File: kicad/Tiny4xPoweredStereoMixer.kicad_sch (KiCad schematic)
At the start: 15 parts, among them J1 RCJ-2221, J2 RCJ-2221, J3 RCJ-2221, J4 RCJ-2221, J5 RCJ-2221, U3 LM2611AMF/NOPB

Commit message: updates
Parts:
- added C7: 100nF, Capacitor_SMD:C_0603_1608Metric_Pad1.08x0.95mm_HandSolder, symbol Device:C
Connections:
- net +12V: now also C7.1
- net GND: now also C7.2
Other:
- moved on the sheet: C1
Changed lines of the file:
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@@
   (junction (at 177.8 58.42) (diameter 0) (color 0 0 0 0)
   )
-  (junction (at 83.82 78.74) (diameter 0) (color 0 0 0 0)
+  (junction (at 62.23 78.74) (diameter 0) (color 0 0 0 0)
   )
   (junction (at 158.75 43.18) (diameter 0) (color 0 0 0 0)
@@
   (junction (at 137.16 68.58) (diameter 0) (color 0 0 0 0)
   )
-  (junction (at 83.82 43.18) (diameter 0) (color 0 0 0 0)
+  (junction (at 80.01 78.74) (diameter 0) (color 0 0 0 0)
+  )
+  (junction (at 62.23 43.18) (diameter 0) (color 0 0 0 0)
   )
   (junction (at 158.75 78.74) (diameter 0) (color 0 0 0 0)
@@
     (stroke (width 0) (type default))
   )
-  (wire (pts (xy 83.82 78.74) (xy 114.3 78.74))
+  (wire (pts (xy 80.01 63.5) (xy 91.44 63.5))
+    (stroke (width 0) (type default))
+  )
+  (wire (pts (xy 80.01 63.5) (xy 80.01 66.04))
+    (stroke (width 0) (type default))
+  )
+  (wire (pts (xy 62.23 78.74) (xy 80.01 78.74))
     (stroke (width 0) (type default))
   )
@@
     (stroke (width 0) (type default))
   )
-  (wire (pts (xy 83.82 59.69) (xy 83.82 78.74))
+  (wire (pts (xy 62.23 59.69) (xy 62.23 78.74))
     (stroke (width 0) (type default))
   )
@@
     (stroke (width 0) (type default))
   )
+  (wire (pts (xy 80.01 73.66) (xy 80.01 78.74))
+    (stroke (width 0) (type default))
+  )
   (wire (pts (xy 46.99 120.65) (xy 76.2 120.65))
     (stroke (width 0) (type default))
@@
     (stroke (width 0) (type default))
   )
-  (wire (pts (xy 83.82 43.18) (xy 83.82 52.07))
+  (wire (pts (xy 62.23 43.18) (xy 62.23 52.07))
     (stroke (width 0) (type default))
   )
@@
     (stroke (width 0) (type default))
   )
-  (wire (pts (xy 83.82 36.83) (xy 83.82 43.18))
+  (wire (pts (xy 62.23 36.83) (xy 62.23 43.18))
     (stroke (width 0) (type default))
   )
@@
     (stroke (width 0) (type default))
   )
-  (wire (pts (xy 83.82 43.18) (xy 91.44 43.18))
+  (wire (pts (xy 80.01 78.74) (xy 114.3 78.74))
+    (stroke (width 0) (type default))
+  )
+  (wire (pts (xy 62.23 43.18) (xy 91.44 43.18))
     (stroke (width 0) (type default))
   )
@@
     )
   )
-  (symbol (lib_id "power:PWR_FLAG") (at 83.82 78.74 180) (unit 1)
-    (in_bom yes) (on_board yes) (dnp no) (fields_autoplaced)
-    (property "Reference" "#FLG01" (at 83.82 80.645 0)
-      (effects (font (size 1.27 1.27)) hide)
-    )
-    (property "Value" "PWR_FLAG" (at 83.82 83.82 0)
-      (effects (font (size 1.27 1.27)))
-    )
-    (property "Footprint" "" (at 83.82 78.74 0)
-      (effects (font (size 1.27 1.27)) hide)
-    )
-    (property "Datasheet" "~" (at 83.82 78.74 0)
+  (symbol (lib_id "power:PWR_FLAG") (at 62.23 78.74 180) (unit 1)
+    (in_bom yes) (on_board yes) (dnp no) (fields_autoplaced)
+    (property "Reference" "#FLG01" (at 62.23 80.645 0)
+      (effects (font (size 1.27 1.27)) hide)
+    )
+    (property "Value" "PWR_FLAG" (at 62.23 83.82 0)
+      (effects (font (size 1.27 1.27)))
+    )
+    (property "Footprint" "" (at 62.23 78.74 0)
+      (effects (font (size 1.27 1.27)) hide)
+    )
+    (property "Datasheet" "~" (at 62.23 78.74 0)
       (effects (font (size 1.27 1.27)) hide)
     )
@@
     )
   )
-  (symbol (lib_id "power:+12V") (at 83.82 36.83 0) (unit 1)
-    (in_bom yes) (on_board yes) (dnp no) (fields_autoplaced)
-    (property "Reference" "#PWR05" (at 83.82 40.64 0)
-      (effects (font (size 1.27 1.27)) hide)
-    )
-    (property "Value" "+12V" (at 83.82 31.75 0)
-      (effects (font (size 1.27 1.27)))
-    )
-    (property "Footprint" "" (at 83.82 36.83 0)
-      (effects (font (size 1.27 1.27)) hide)
-    )
-    (property "Datasheet" "" (at 83.82 36.83 0)
+  (symbol (lib_id "power:+12V") (at 62.23 36.83 0) (unit 1)
+    (in_bom yes) (on_board yes) (dnp no) (fields_autoplaced)
+    (property "Reference" "#PWR05" (at 62.23 40.64 0)
+      (effects (font (size 1.27 1.27)) hide)
+    )
+    (property "Value" "+12V" (at 62.23 31.75 0)
+      (effects (font (size 1.27 1.27)))
+    )
+    (property "Footprint" "" (at 62.23 36.83 0)
+      (effects (font (size 1.27 1.27)) hide)
+    )
+    (property "Datasheet" "" (at 62.23 36.83 0)
       (effects (font (size 1.27 1.27)) hide)
     )
@@
     )
   )
-  (symbol (lib_id "Device:C") (at 83.82 55.88 0) (mirror x) (unit 1)
+  (symbol (lib_id "Device:C") (at 62.23 55.88 0) (mirror x) (unit 1)
     (in_bom yes) (on_board yes) (dnp no)
-    (property "Reference" "C1" (at 80.01 54.61 0)
+    (property "Reference" "C1" (at 58.42 54.61 0)
       (effects (font (size 1.27 1.27)) (justify right))
     )
-    (property "Value" "22u" (at 80.01 57.15 0)
+    (property "Value" "22u" (at 58.42 57.15 0)
       (effects (font (size 1.27 1.27)) (justify right))
     )
-    (property "Footprint" "Capacitor_SMD:C_1210_3225Metric_Pad1.33x2.70mm_HandSolder" (at 84.7852 52.07 0)
-      (effects (font (size 1.27 1.27)) hide)
-    )
-    (property "Datasheet" "https://datasheet.lcsc.com/lcsc/2304140030_Samsung-Electro-Mechanics-CL32A226KAJNNNE_C52306.pdf" (at 83.82 55.88 0)
-      (effects (font (size 1.27 1.27)) hide)
-    )
-    (property "Notes" "X5R 25V" (at 78.74 59.69 0)
-      (effects (font (size 1.27 1.27)))
-    )
-    (property "LCSC" "C52306" (at 83.82 55.88 0)
-      (effects (font (size 1.27 1.27)) hide)
-    )
-    (property "Mouser" "" (at 83.82 55.88 0)
+    (property "Footprint" "Capacitor_SMD:C_1210_3225Metric_Pad1.33x2.70mm_HandSolder" (at 63.1952 52.07 0)
+      (effects (font (size 1.27 1.27)) hide)
+    )
+    (property "Datasheet" "https://datasheet.lcsc.com/lcsc/2304140030_Samsung-Electro-Mechanics-CL32A226KAJNNNE_C52306.pdf" (at 62.23 55.88 0)
+      (effects (font (size 1.27 1.27)) hide)
+    )
+    (property "Notes" "X5R 25V" (at 57.15 59.69 0)
+      (effects (font (size 1.27 1.27)))
+    )
+    (property "LCSC" "C52306" (at 62.23 55.88 0)
+      (effects (font (size 1.27 1.27)) hide)
+    )
+    (property "Mouser" "" (at 62.23 55.88 0)
       (effects (font (size 1.27 1.27)) hide)
     )
@@
         )
       )
+    )
+  )
+  (symbol (lib_id "Device:C") (at 80.01 69.85 0) (mirror y) (unit 1)
+    (in_bom yes) (on_board yes) (dnp no)
+    (property "Reference" "C7" (at 76.2 68.58 0)
+      (effects (font (size 1.27 1.27)) (justify left))
+    )
+    (property "Value" "100nF" (at 76.2 71.12 0)
+      (effects (font (size 1.27 1.27)) (justify left))
+    )
+    (property "Footprint" "Capacitor_SMD:C_0603_1608Metric_Pad1.08x0.95mm_HandSolder" (at 79.0448 73.66 0)
+      (effects (font (size 1.27 1.27)) hide)
+    )
+    (property "Datasheet" "https://datasheet.lcsc.com/lcsc/2304140030_Samsung-Electro-Mechanics-CL10B104KA8NNNC_C1590.pdf" (at 80.01 69.85 0)
+      (effects (font (size 1.27 1.27)) hide)
+    )
+    (property "LCSC" "C1590" (at 80.01 69.85 0)
+      (effects (font (size 1.27 1.27)) hide)
+    )
+    (property "Notes" "X7R 25V" (at 80.01 69.85 0)
+      (effects (font (size 1.27 1.27)) hide)
+    )
+    (property "Mouser" "" (at 80.01 69.85 0)
+      (effects (font (size 1.27 1.27)) hide)
+    )
+    (pin "1")
+    (pin "2")
+    (instances
+      (project "Tiny4xPoweredStereoMixer"
+        (path "/68c4b081-ef47-4ba5-a55f-4ef66cb2b598/f21b05ca-c53e-4c9f-92f9-42535cdfa7f7"
+          (reference "C7") (unit 1)
+        )
+        (path "/68c4b081-ef47-4ba5-a55f-4ef66cb2b598/552f3912-3928-454a-823e-6f183577fda8"
+          (reference "C5") (unit 1)
+        )
+        (path "/68c4b081-ef47-4ba5-a55f-4ef66cb2b598/4f5d350b-a08e-4f50-b16f-b5f92c91b503"
+          (reference "C11") (unit 1)
+        )
+        (path "/68c4b081-ef47-4ba5-a55f-4ef66cb2b598/bfd1c0ad-a46f-412b-810b-077847d96983"
+          (reference "C13") (unit 1)
+        )
+        (path "/68c4b081-ef47-4ba5-a55f-4ef66cb2b598"
+          (reference "C15") (unit 1)
+        )
+      )

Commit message: saved
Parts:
- renumbered C7 to C15, U3 to U6
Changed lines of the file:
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@@
   (symbol (lib_id "Device:C") (at 80.01 69.85 0) (mirror y) (unit 1)
     (in_bom yes) (on_board yes) (dnp no)
-    (property "Reference" "C7" (at 76.2 68.58 0)
+    (property "Reference" "C15" (at 76.2 68.58 0)
       (effects (font (size 1.27 1.27)) (justify left))
     )
@@
     (instances
       (project "Tiny4xPoweredStereoMixer"
-        (path "/68c4b081-ef47-4ba5-a55f-4ef66cb2b598/f21b05ca-c53e-4c9f-92f9-42535cdfa7f7"
-          (reference "C7") (unit 1)
-        )
-        (path "/68c4b081-ef47-4ba5-a55f-4ef66cb2b598/552f3912-3928-454a-823e-6f183577fda8"
-          (reference "C5") (unit 1)
-        )
-        (path "/68c4b081-ef47-4ba5-a55f-4ef66cb2b598/4f5d350b-a08e-4f50-b16f-b5f92c91b503"
-          (reference "C11") (unit 1)
-        )
-        (path "/68c4b081-ef47-4ba5-a55f-4ef66cb2b598/bfd1c0ad-a46f-412b-810b-077847d96983"
-          (reference "C13") (unit 1)
-        )
         (path "/68c4b081-ef47-4ba5-a55f-4ef66cb2b598"
           (reference "C15") (unit 1)
@@
   (symbol (lib_id "Regulator_Switching:LM2611xMF") (at 114.3 66.04 0) (unit 1)
     (in_bom yes) (on_board yes) (dnp no) (fields_autoplaced)
-    (property "Reference" "U3" (at 114.3 55.88 0)
+    (property "Reference" "U6" (at 114.3 55.88 0)
       (effects (font (size 1.27 1.27)))
     )
@@
     (instances
       (project "Tiny4xPoweredStereoMixer"
-        (path "/68c4b081-ef47-4ba5-a55f-4ef66cb2b598/f21b05ca-c53e-4c9f-92f9-42535cdfa7f7"
-          (reference "U3") (unit 1)
-        )
         (path "/68c4b081-ef47-4ba5-a55f-4ef66cb2b598"
           (reference "U6") (unit 1)

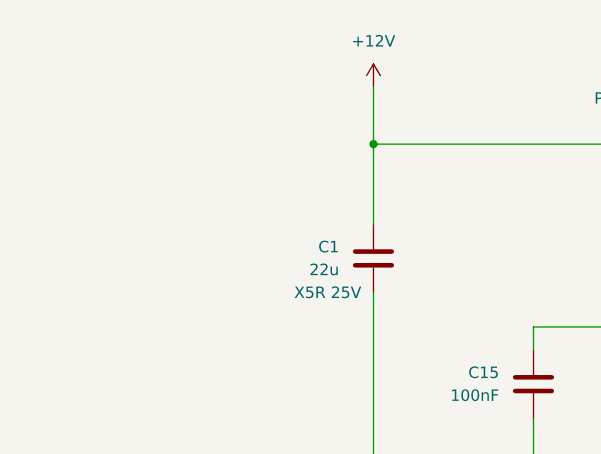
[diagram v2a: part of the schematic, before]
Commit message: added barrel jack connector to schema
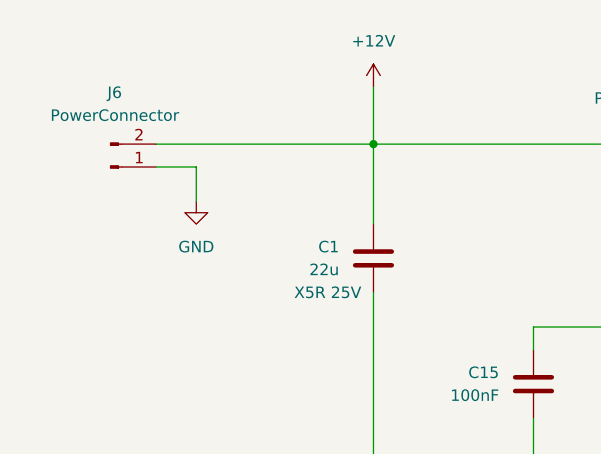
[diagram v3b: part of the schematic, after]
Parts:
- added J6: PowerConnector, Connector_PinHeader_2.54mm:PinHeader_1x02_P2.54mm_Vertical, symbol Connector:Conn_01x02_Pin
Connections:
- net +12V: now also J6.2 (Pin_2)
- net GND: now also J6.1 (Pin_1)
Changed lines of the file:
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@@
+    (stroke (width 0) (type default))
+  )
+  (wire (pts (xy 38.1 43.18) (xy 62.23 43.18))
     (stroke (width 0) (type default))
   )
@@
     (stroke (width 0) (type default))
   )
+  (wire (pts (xy 42.545 45.72) (xy 42.545 49.53))
+    (stroke (width 0) (type default))
+  )
   (wire (pts (xy 91.44 43.18) (xy 110.49 43.18))
     (stroke (width 0) (type default))
@@
   )
   (wire (pts (xy 46.99 105.41) (xy 76.2 105.41))
+    (stroke (width 0) (type default))
+  )
+  (wire (pts (xy 38.1 45.72) (xy 42.545 45.72))
     (stroke (width 0) (type default))
   )
@@
     )
   )
+  (symbol (lib_id "Connector:Conn_01x02_Pin") (at 33.02 45.72 0) (mirror x) (unit 1)
+    (in_bom yes) (on_board yes) (dnp no)
+    (property "Reference" "J6" (at 34.29 37.465 0)
+      (effects (font (size 1.27 1.27)) (justify right))
+    )
+    (property "Value" "PowerConnector" (at 40.64 40.005 0)
+      (effects (font (size 1.27 1.27)) (justify right))
+    )
+    (property "Footprint" "Connector_PinHeader_2.54mm:PinHeader_1x02_P2.54mm_Vertical" (at 33.02 45.72 0)
+      (effects (font (size 1.27 1.27)) hide)
+    )
+    (property "Datasheet" "~" (at 33.02 45.72 0)
+      (effects (font (size 1.27 1.27)) hide)
+    )
+    (pin "1")
+    (pin "2")
+    (instances
+      (project "Tiny4xPoweredStereoMixer"
+        (path "/68c4b081-ef47-4ba5-a55f-4ef66cb2b598"
+          (reference "J6") (unit 1)
+        )
+      )
+    )
+  )
   (symbol (lib_id "power:+12V") (at 62.23 36.83 0) (unit 1)
     (in_bom yes) (on_board yes) (dnp no) (fields_autoplaced)
@@
         )
       )
+    )
+  )
+  (symbol (lib_id "power:GND") (at 42.545 49.53 0) (unit 1)
+    (in_bom yes) (on_board yes) (dnp no) (fields_autoplaced)
+    (property "Reference" "#PWR044" (at 42.545 55.88 0)
+      (effects (font (size 1.27 1.27)) hide)
+    )
+    (property "Value" "GND" (at 42.545 54.61 0)
+      (effects (font (size 1.27 1.27)))
+    )
+    (property "Footprint" "" (at 42.545 49.53 0)
+      (effects (font (size 1.27 1.27)) hide)
+    )
+    (property "Datasheet" "" (at 42.545 49.53 0)
+      (effects (font (size 1.27 1.27)) hide)
+    )
+    (pin "1")
+    (instances
+      (project "Tiny4xPoweredStereoMixer"
+        (path "/68c4b081-ef47-4ba5-a55f-4ef66cb2b598"
+          (reference "#PWR044") (unit 1)
+        )
+      )

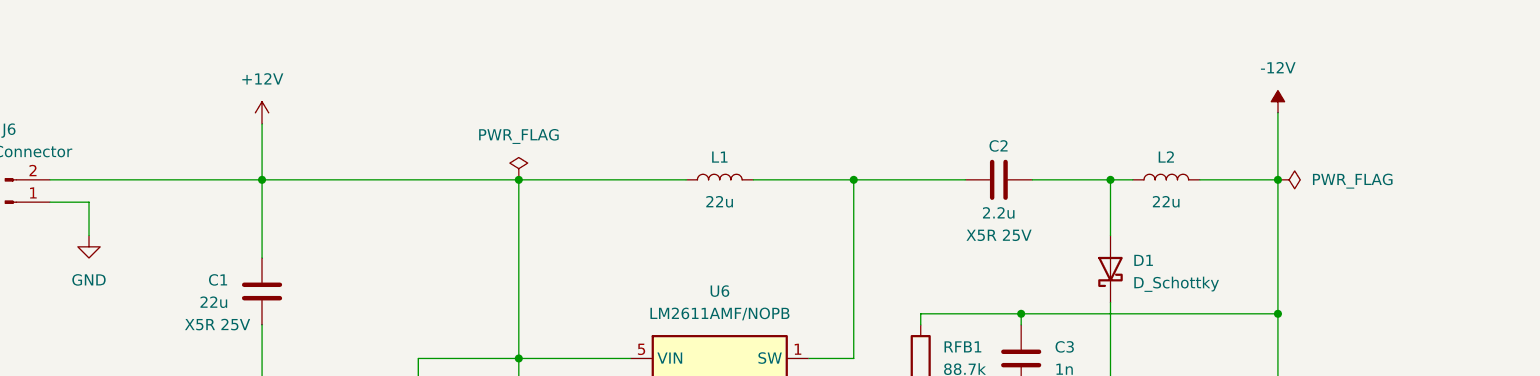
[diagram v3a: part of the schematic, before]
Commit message: added connectors/jumper for isolating the +/-12V power lines
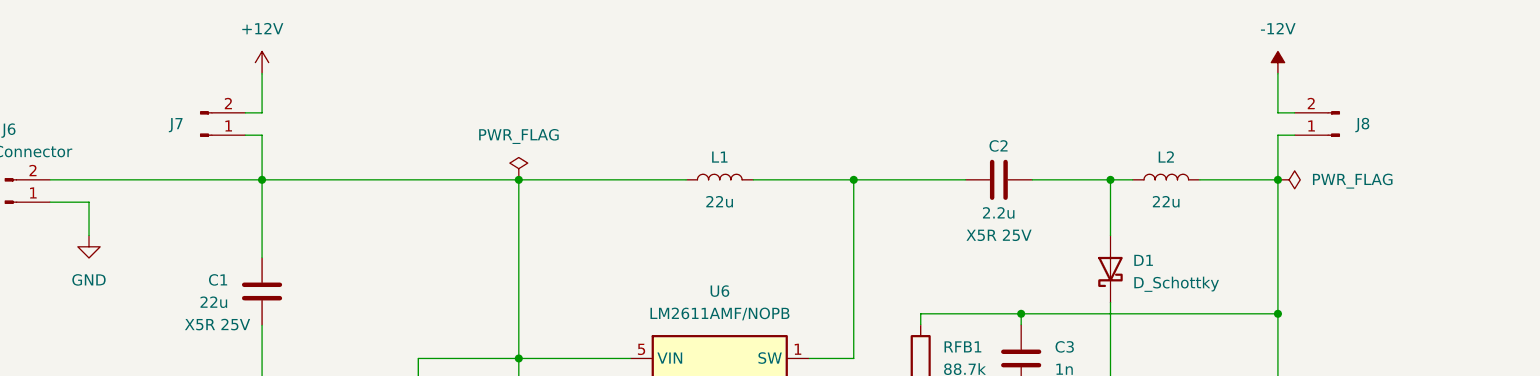
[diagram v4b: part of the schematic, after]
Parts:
- added J7, J8: PowerConnector, Connector_PinHeader_2.54mm:PinHeader_1x02_P2.54mm_Vertical, symbol Connector:Conn_01x02_Pin
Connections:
- net +12V: now also J7.2 (Pin_2); no longer C1.2, C15.1, J6.2 (Pin_2), L1.1, U6.4 (~{SHDN}), U6.5 (VIN)
- net -12V: now also J8.2 (Pin_2); no longer C3.2, C4.2, L2.2, RFB1.1
- new net: C3.2, C4.2, J8.1 (Pin_1), L2.2, RFB1.1
- new net: C1.2, C15.1, J6.2 (Pin_2), J7.1 (Pin_1), L1.1, U6.4 (~{SHDN}), U6.5 (VIN)
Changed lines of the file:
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@@
-    (stroke (width 0) (type default))
-  )
-  (wire (pts (xy 177.8 35.56) (xy 177.8 43.18))
     (stroke (width 0) (type default))
   )
@@
     (stroke (width 0) (type default))
   )
+  (wire (pts (xy 60.325 35.56) (xy 62.23 35.56))
+    (stroke (width 0) (type default))
+  )
   (wire (pts (xy 201.93 127) (xy 236.22 127))
     (stroke (width 0) (type default))
@@
     (stroke (width 0) (type default))
   )
+  (wire (pts (xy 62.23 38.1) (xy 62.23 43.18))
+    (stroke (width 0) (type default))
+  )
   (wire (pts (xy 148.59 58.42) (xy 177.8 58.42))
     (stroke (width 0) (type default))
@@
     (stroke (width 0) (type default))
   )
+  (wire (pts (xy 179.705 38.1) (xy 177.8 38.1))
+    (stroke (width 0) (type default))
+  )
   (wire (pts (xy 46.99 135.89) (xy 76.2 135.89))
     (stroke (width 0) (type default))
@@
     (stroke (width 0) (type default))
   )
+  (wire (pts (xy 177.8 38.1) (xy 177.8 43.18))
+    (stroke (width 0) (type default))
+  )
   (wire (pts (xy 46.99 151.13) (xy 76.2 151.13))
     (stroke (width 0) (type default))
   )
+  (wire (pts (xy 60.325 38.1) (xy 62.23 38.1))
+    (stroke (width 0) (type default))
+  )
   (wire (pts (xy 149.86 43.18) (xy 158.75 43.18))
     (stroke (width 0) (type default))
@@
     (stroke (width 0) (type default))
   )
-  (wire (pts (xy 62.23 36.83) (xy 62.23 43.18))
-    (stroke (width 0) (type default))
-  )
   (wire (pts (xy 46.99 110.49) (xy 49.53 110.49))
     (stroke (width 0) (type default))
   )
+  (wire (pts (xy 177.8 35.56) (xy 177.8 31.115))
+    (stroke (width 0) (type default))
+  )
   (wire (pts (xy 129.54 43.18) (xy 129.54 63.5))
     (stroke (width 0) (type default))
   )
+  (wire (pts (xy 62.23 35.56) (xy 62.23 31.115))
+    (stroke (width 0) (type default))
+  )
   (wire (pts (xy 80.01 78.74) (xy 114.3 78.74))
     (stroke (width 0) (type default))
@@
   )
   (wire (pts (xy 129.54 43.18) (xy 142.24 43.18))
+    (stroke (width 0) (type default))
+  )
+  (wire (pts (xy 179.705 35.56) (xy 177.8 35.56))
     (stroke (width 0) (type default))
   )
@@
     )
   )
-  (symbol (lib_id "power:+12V") (at 62.23 36.83 0) (unit 1)
-    (in_bom yes) (on_board yes) (dnp no) (fields_autoplaced)
-    (property "Reference" "#PWR05" (at 62.23 40.64 0)
-      (effects (font (size 1.27 1.27)) hide)
-    )
-    (property "Value" "+12V" (at 62.23 31.75 0)
-      (effects (font (size 1.27 1.27)))
-    )
-    (property "Footprint" "" (at 62.23 36.83 0)
-      (effects (font (size 1.27 1.27)) hide)
-    )
-    (property "Datasheet" "" (at 62.23 36.83 0)
+  (symbol (lib_id "power:+12V") (at 62.23 31.115 0) (unit 1)
+    (in_bom yes) (on_board yes) (dnp no) (fields_autoplaced)
+    (property "Reference" "#PWR05" (at 62.23 34.925 0)
+      (effects (font (size 1.27 1.27)) hide)
+    )
+    (property "Value" "+12V" (at 62.23 26.035 0)
+      (effects (font (size 1.27 1.27)))
+    )
+    (property "Footprint" "" (at 62.23 31.115 0)
+      (effects (font (size 1.27 1.27)) hide)
+    )
+    (property "Datasheet" "" (at 62.23 31.115 0)
       (effects (font (size 1.27 1.27)) hide)
     )
@@
     )
   )
+  (symbol (lib_id "Connector:Conn_01x02_Pin") (at 55.245 38.1 0) (mirror x) (unit 1)
+    (in_bom yes) (on_board yes) (dnp no)
+    (property "Reference" "J7" (at 53.34 36.83 0)
+      (effects (font (size 1.27 1.27)) (justify right))
+    )
+    (property "Value" "PowerConnector" (at 62.865 32.385 0)
+      (effects (font (size 1.27 1.27)) (justify right) hide)
+    )
+    (property "Footprint" "Connector_PinHeader_2.54mm:PinHeader_1x02_P2.54mm_Vertical" (at 55.245 38.1 0)
+      (effects (font (size 1.27 1.27)) hide)
+    )
+    (property "Datasheet" "~" (at 55.245 38.1 0)
+      (effects (font (size 1.27 1.27)) hide)
+    )
+    (pin "1")
+    (pin "2")
+    (instances
+      (project "Tiny4xPoweredStereoMixer"
+        (path "/68c4b081-ef47-4ba5-a55f-4ef66cb2b598"
+          (reference "J7") (unit 1)
+        )
+      )
+    )
+  )
   (symbol (lib_id "Device:C") (at 148.59 63.5 180) (unit 1)
     (in_bom yes) (on_board yes) (dnp no) (fields_autoplaced)
@@
     )
   )
-  (symbol (lib_id "power:-12V") (at 177.8 35.56 0) (unit 1)
-    (in_bom yes) (on_board yes) (dnp no) (fields_autoplaced)
-    (property "Reference" "#PWR07" (at 177.8 33.02 0)
-      (effects (font (size 1.27 1.27)) hide)
-    )
-    (property "Value" "-12V" (at 177.8 30.48 0)
-      (effects (font (size 1.27 1.27)))
-    )
-    (property "Footprint" "" (at 177.8 35.56 0)
-      (effects (font (size 1.27 1.27)) hide)
-    )
-    (property "Datasheet" "" (at 177.8 35.56 0)
+  (symbol (lib_id "power:-12V") (at 177.8 31.115 0) (unit 1)
+    (in_bom yes) (on_board yes) (dnp no) (fields_autoplaced)
+    (property "Reference" "#PWR07" (at 177.8 28.575 0)
+      (effects (font (size 1.27 1.27)) hide)
+    )
+    (property "Value" "-12V" (at 177.8 26.035 0)
+      (effects (font (size 1.27 1.27)))
+    )
+    (property "Footprint" "" (at 177.8 31.115 0)
+      (effects (font (size 1.27 1.27)) hide)
+    )
+    (property "Datasheet" "" (at 177.8 31.115 0)
       (effects (font (size 1.27 1.27)) hide)
     )
@@
         )
       )
+    )
+  )
+  (symbol (lib_id "Connector:Conn_01x02_Pin") (at 184.785 38.1 180) (unit 1)
+    (in_bom yes) (on_board yes) (dnp no)
+    (property "Reference" "J8" (at 186.69 36.83 0)
+      (effects (font (size 1.27 1.27)) (justify right))
+    )
+    (property "Value" "PowerConnector" (at 177.165 32.385 0)
+      (effects (font (size 1.27 1.27)) (justify right) hide)
+    )
+    (property "Footprint" "Connector_PinHeader_2.54mm:PinHeader_1x02_P2.54mm_Vertical" (at 184.785 38.1 0)
+      (effects (font (size 1.27 1.27)) hide)
+    )
+    (property "Datasheet" "~" (at 184.785 38.1 0)
+      (effects (font (size 1.27 1.27)) hide)
+    )
+    (pin "1")
+    (pin "2")
+    (instances
+      (project "Tiny4xPoweredStereoMixer"
+        (path "/68c4b081-ef47-4ba5-a55f-4ef66cb2b598"
+          (reference "J8") (unit 1)
+        )
+      )
